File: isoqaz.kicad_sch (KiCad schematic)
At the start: 21 parts, among them J1 USB_C_Receptacle_USB2.0, U1 STM32F072CBT6, U2 PRTR5V0U2X, U3 XC6206PxxxMR-Regulator_Linear

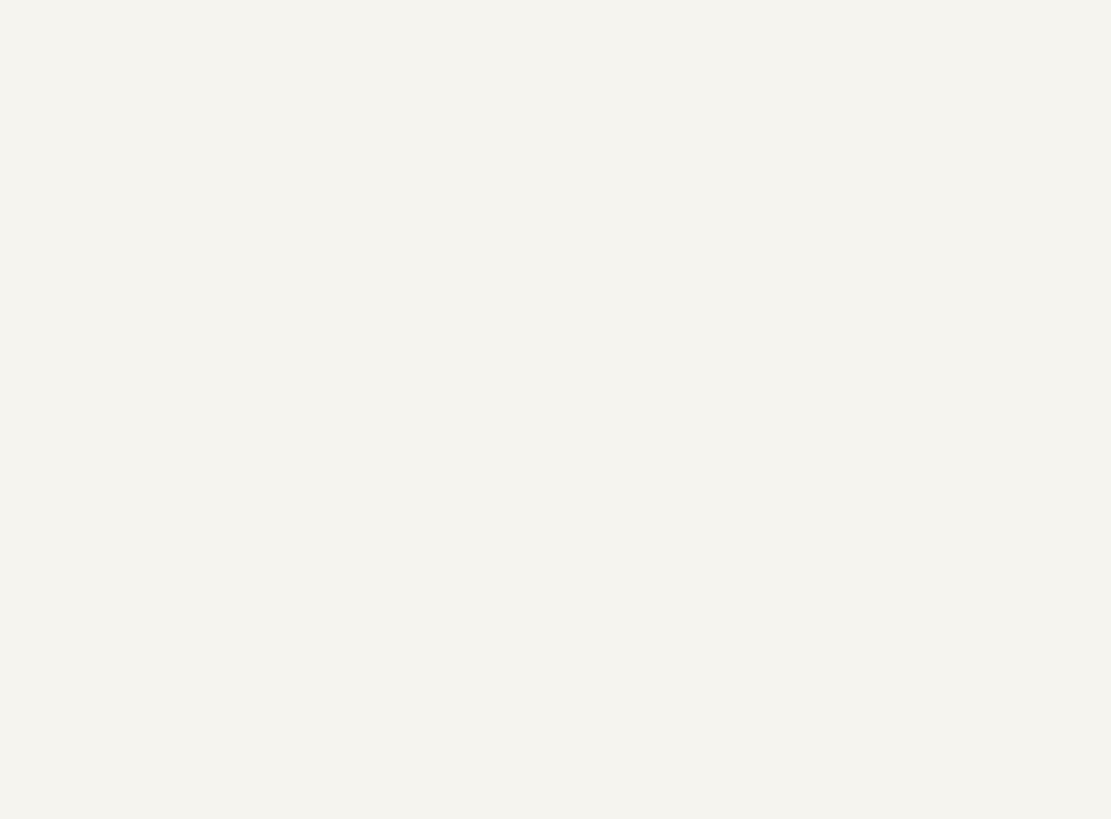
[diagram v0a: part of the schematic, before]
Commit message: added case files, finished pcb
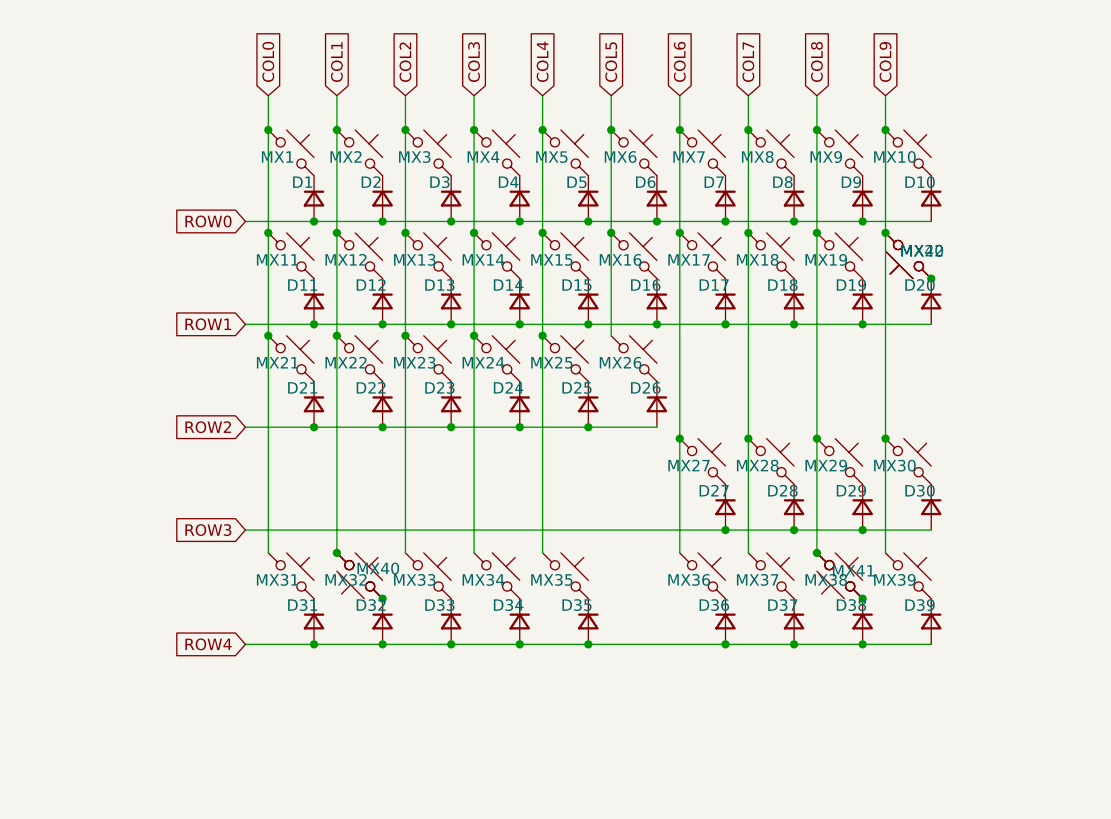
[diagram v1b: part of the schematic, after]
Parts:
- added D1, D10, D11, D12, D13, D14, D15, D16, D17, D18, D19, D2, D20, D21, D22, D23, D24, D25, D26, D27, D28, D29, D3, D30, D31, D32, D33, D34, D35, D36, D37, D38, D39, D4, D5, D6, D7, D8, D9: D_Small, Diode_SMD:D_SOD-123, symbol Device:D_Small
- added MX1, MX10, MX11, MX12, MX13, MX14, MX15, MX16, MX17, MX18, MX19, MX2, MX20, MX21, MX22, MX23, MX24, MX25, MX26, MX27, MX28, MX29, MX3, MX30, MX31, MX32, MX33, MX34, MX35, MX36, MX37, MX38, MX39, MX4, MX40, MX41, MX42, MX5, MX6, MX7, MX8, MX9: MX_SW_HS, marbastlib-mx:SW_MX_HS_CPG151101S11_1u, symbol marbastlib-mx:MX_SW_HS_CPG151101S11
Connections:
- new net: D35.1 (K), MX35.2
- new net: D32.1 (K), MX32.2, MX40.1
- new net: D2.1 (K), MX2.2
- new net: D22.1 (K), MX22.2
- new net: D18.1 (K), MX18.2
- new net: D3.1 (K), MX3.2
- new net: D36.1 (K), MX36.2
- new net: D14.1 (K), MX14.2
- new net: D9.1 (K), MX9.2
- new net: D15.1 (K), MX15.2
- new net: D21.1 (K), MX21.2
- new net: D19.1 (K), MX19.2
- new net: D33.1 (K), MX33.2
- new net: D37.1 (K), MX37.2
- new net: D7.1 (K), MX7.2
- new net: D13.1 (K), MX13.2
- new net: D26.1 (K), MX26.2
- new net: D20.1 (K), MX20.1, MX42.1
- new net: D6.1 (K), MX6.2
- new net: D27.1 (K), MX27.2
- new net: D12.1 (K), MX12.2
- new net: D24.1 (K), MX24.2
- new net: D34.1 (K), MX34.2
- new net: D8.1 (K), MX8.2
- new net: D39.1 (K), MX39.2
- new net: D29.1 (K), MX29.2
- new net: D28.1 (K), MX28.2
- new net: D25.1 (K), MX25.2
- new net: D31.1 (K), MX31.2
- new net: D30.1 (K), MX30.2
- new net: D4.1 (K), MX4.2
- new net: D10.1 (K), MX10.2
- new net: D5.1 (K), MX5.2
- new net: D11.1 (K), MX11.2
- new net: D38.1 (K), MX38.2, MX41.1
- new net: D16.1 (K), MX16.2
- new net: D23.1 (K), MX23.2
- new net: D17.1 (K), MX17.2
- new net: D1.1 (K), MX1.2
- new net COL0: MX1.1, MX11.1, MX21.1, MX31.1
- new net COL1: MX12.1, MX2.1, MX22.1, MX32.1, MX40.2
- new net COL2: MX13.1, MX23.1, MX3.1, MX33.1
- new net COL3: MX14.1, MX24.1, MX34.1, MX4.1
- new net COL4: MX15.1, MX25.1, MX35.1, MX5.1
- new net COL5: MX16.1, MX26.1, MX6.1
- new net COL6: MX17.1, MX27.1, MX36.1, MX7.1
- new net COL7: MX18.1, MX28.1, MX37.1, MX8.1
- new net COL8: MX19.1, MX29.1, MX38.1, MX41.2, MX9.1
- new net COL9: MX10.1, MX20.2, MX30.1, MX39.1, MX42.2
- new net ROW0: D1.2 (A), D10.2 (A), D2.2 (A), D3.2 (A), D4.2 (A), D5.2 (A), D6.2 (A), D7.2 (A), D8.2 (A), D9.2 (A)
- new net ROW1: D11.2 (A), D12.2 (A), D13.2 (A), D14.2 (A), D15.2 (A), D16.2 (A), D17.2 (A), D18.2 (A), D19.2 (A), D20.2 (A)
- new net ROW2: D21.2 (A), D22.2 (A), D23.2 (A), D24.2 (A), D25.2 (A), D26.2 (A)
- new net ROW3: D27.2 (A), D28.2 (A), D29.2 (A), D30.2 (A)
- new net ROW4: D31.2 (A), D32.2 (A), D33.2 (A), D34.2 (A), D35.2 (A), D36.2 (A), D37.2 (A), D38.2 (A), D39.2 (A)
